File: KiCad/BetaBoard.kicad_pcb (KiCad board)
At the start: 2 copper layers, 40 parts, among them J1 RJ45, J10 CTB9308/4, J11 CTB9308/4, J12 CTB9308/4, J13 CTB9308/4, J14 CTB9308/4, J15 CTB9308/4, J16 CTB9308/4, J17 CTB9308/4, J18 CTB9308/4, J19 CTB9308/4, J2 RJ45, J20 CTB9308/4, J21 CTB9308/4, J22 CTB9308/4, J23 CTB9308/4, J24 CTB9308/4, J25 CTB9308/4, J26 CTB9308/4, J27 CTB9308/4, J28 CTB9308/4, J29 CTB9308/4, J3 CTB9308/4, J30 CTB9308/4, J31 CTB9308/4, J32 CTB9308/4, J33 CTB9308/4, J34 CTB9308/4, J4 CTB9308/4, J5 CTB9308/4, J6 CTB9308/4, J7 CTB9308/4, J8 CTB9308/4, J9 CTB9308/4, U1 74HC04, U2 ATMEGA328P-PU, U3 A6T-8104, U4 SP485R, U5 74HC154, U6 74HC154

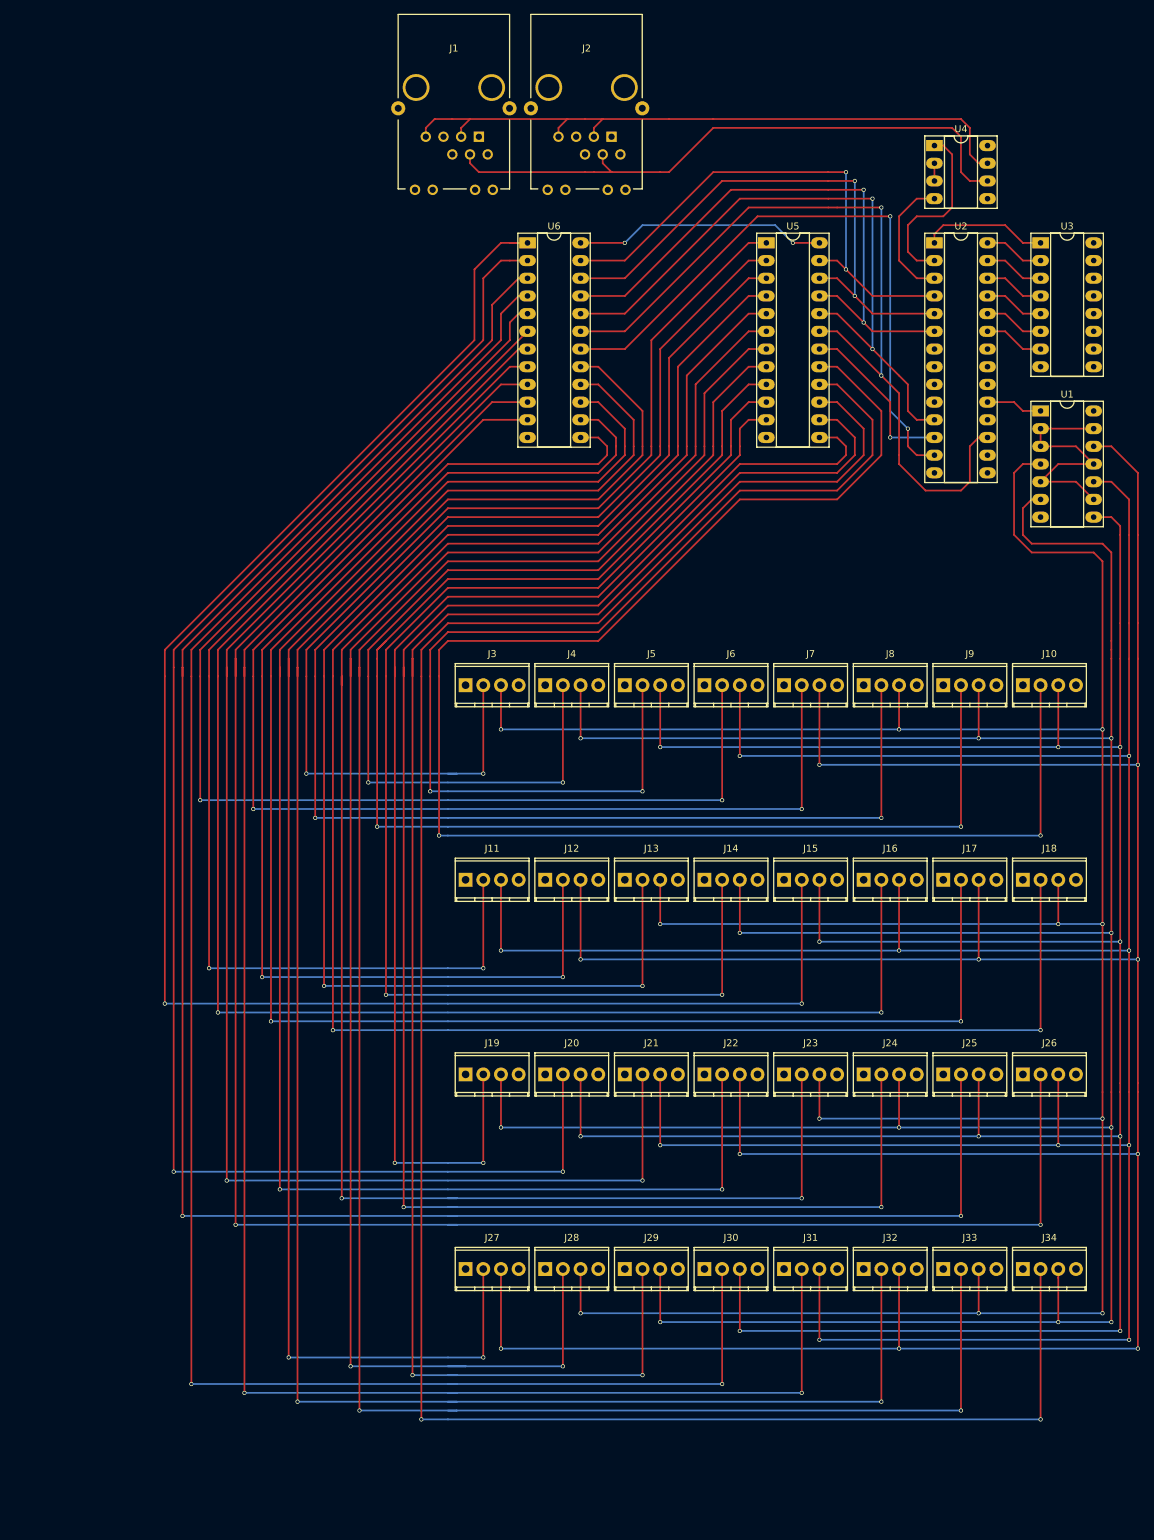
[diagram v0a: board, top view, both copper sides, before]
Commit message: +Silkscreen/EdgeCuts *DRM Fails
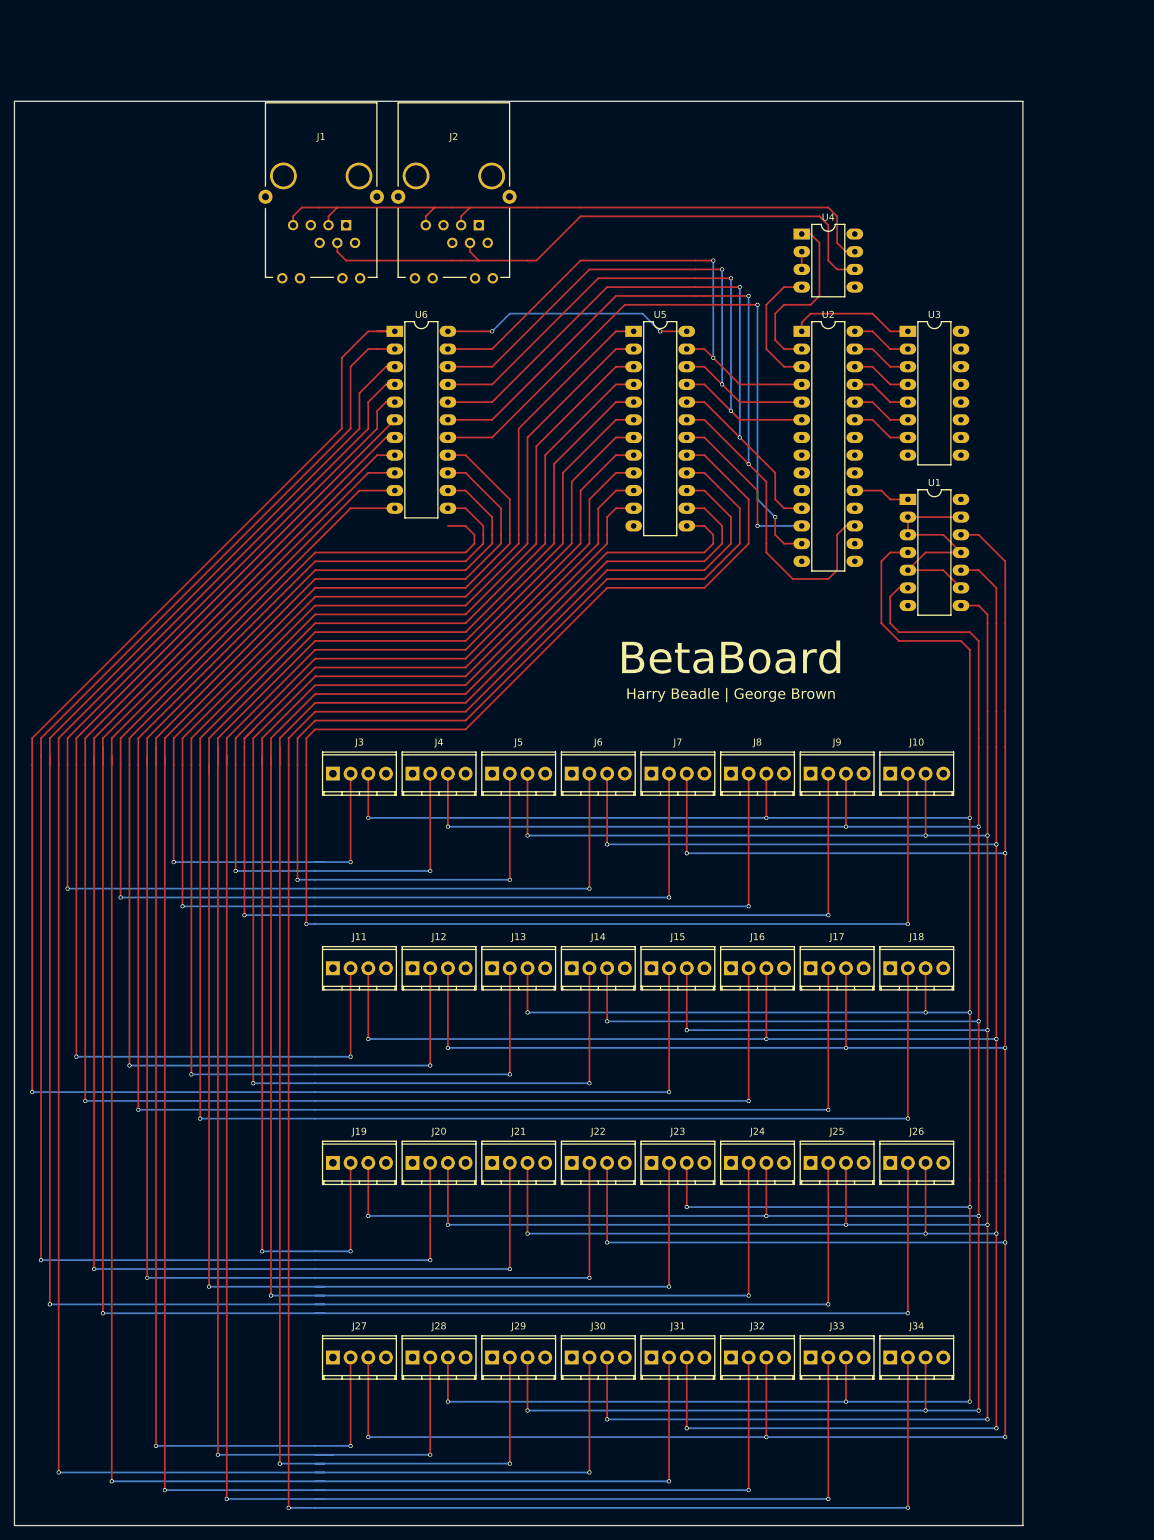
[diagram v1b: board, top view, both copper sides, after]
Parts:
- U1: footprint Housings_DIP:DIP-14_W7.62mm_Socket_LongPads -> Housings_DIP:DIP-14_W7.62mm_LongPads
- U2: footprint Housings_DIP:DIP-28_W7.62mm_Socket_LongPads -> Housings_DIP:DIP-28_W7.62mm_LongPads
- U3: footprint Housings_DIP:DIP-16_W7.62mm_Socket_LongPads -> Housings_DIP:DIP-16_W7.62mm_LongPads
- U4: footprint Housings_DIP:DIP-8_W7.62mm_Socket_LongPads -> Housings_DIP:DIP-8_W7.62mm_LongPads
- U5: footprint Housings_DIP:DIP-24_W7.62mm_Socket_LongPads -> Housings_DIP:DIP-24_W7.62mm_LongPads
- U6: footprint Housings_DIP:DIP-24_W7.62mm_Socket_LongPads -> Housings_DIP:DIP-22_W7.62mm_LongPads
- moved J4 22.9 mm to (87.6, 127.0)
- moved J8 22.9 mm to (133.3, 127.0)
- moved J9 22.9 mm to (144.8, 127.0)
- moved U2 22.9 mm to (143.5, 63.5)
- moved U3 22.9 mm to (158.8, 63.5)
- moved U4 22.9 mm to (143.5, 49.5)
- moved U5 22.9 mm to (119.4, 63.5)
- moved J12 22.9 mm to (87.6, 154.9)
- moved J16 22.9 mm to (133.3, 154.9)
- moved J17 22.9 mm to (144.8, 154.9)
- moved J20 22.9 mm to (87.6, 182.9)
- moved J24 22.9 mm to (133.3, 182.9)
- moved J25 22.9 mm to (144.8, 182.9)
- moved J28 22.9 mm to (87.6, 210.8)
- moved J3 22.9 mm to (76.2, 127.0)
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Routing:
- net GND: track 0.00 -> 222.2 mm, vias 0 -> 2
- net DATA27: track 170.8 -> 385.9 mm, vias 2 -> 3
- net DATA30: track 220.7 -> 100.9 mm, vias 2 -> 3
- net DATA31: track 292.3 -> 178.7 mm, vias 2 -> 3
- net /A0: track 75.9 -> 32.6 mm
- net /~G: track 90.7 -> 47.5 mm, vias 2 -> 0
- net /A1: track 80.3 -> 41.5 mm
- net DATAR: track 120.4 -> 89.0 mm
- net /A2: track 84.6 -> 62.0 mm, vias 2 -> 0
- net DATA28: track 242.5 -> 228.3 mm, vias 2 -> 1
- net VCC: track 36.4 -> 30.0 mm
- net DATA29: track 231.6 -> 227.6 mm
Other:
- board outline added: 144.8 x 204.5 mm
- board text added: "BetaBoard"
- board text added: "Harry Beadle | George Brown"
